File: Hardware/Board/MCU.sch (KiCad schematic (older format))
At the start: 27 parts

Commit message: Wago und FPC Libs zugefügt
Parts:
- added J?: 1-1734592-2, SamacSys_Parts:1-1734592-2, symbol SamacSys_Parts:1-1734592-2
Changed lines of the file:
@@
 Wire Wire Line
 	9300 4850 9300 4800
+$Comp
+L SamacSys_Parts:1-1734592-2 J?
+U 1 1 5CB67827
+P 7500 3050
+F 0 "J?" H 8000 3315 50  0000 C CNN
+F 1 "1-1734592-2" H 8000 3224 50  0000 C CNN
+F 2 "SamacSys_Parts:1-1734592-2" H 8350 3150 50  0001 L CNN
+F 3 "https://www.te.com/commerce/DocumentDelivery/DDEController?Action=showdoc&DocId=Customer+Drawing%7F1734592%7FC%7Fpdf%7FEnglish%7FENG_CD_1734592_C_C_1734592.pdf%7F1-1734592-2" H 8350 3050 50  0001 L CNN
+F 4 "TE Connectivity 0.5mm Pitch 12 Way Right Angle Female FPC Connector Locking Mechanism" H 8350 2950 50  0001 L CNN "Description"
+F 5 "2.3" H 8350 2850 50  0001 L CNN "Height"
+F 6 "TE Connectivity" H 8350 2750 50  0001 L CNN "Manufacturer_Name"
+F 7 "1-1734592-2" H 8350 2650 50  0001 L CNN "Manufacturer_Part_Number"
+F 8 "571-1-1734592-2" H 8350 2550 50  0001 L CNN "Mouser Part Number"
+F 9 "https://www.mouser.com/Search/Refine.aspx?Keyword=571-1-1734592-2" H 8350 2450 50  0001 L CNN "Mouser Price/Stock"
+F 10 "7188602" H 8350 2350 50  0001 L CNN "RS Part Number"
+F 11 "http://uk.rs-online.com/web/p/products/7188602" H 8350 2250 50  0001 L CNN "RS Price/Stock"
+	1    7500 3050
+	1    0    0    -1
+$EndComp
 $EndSCHEMATC

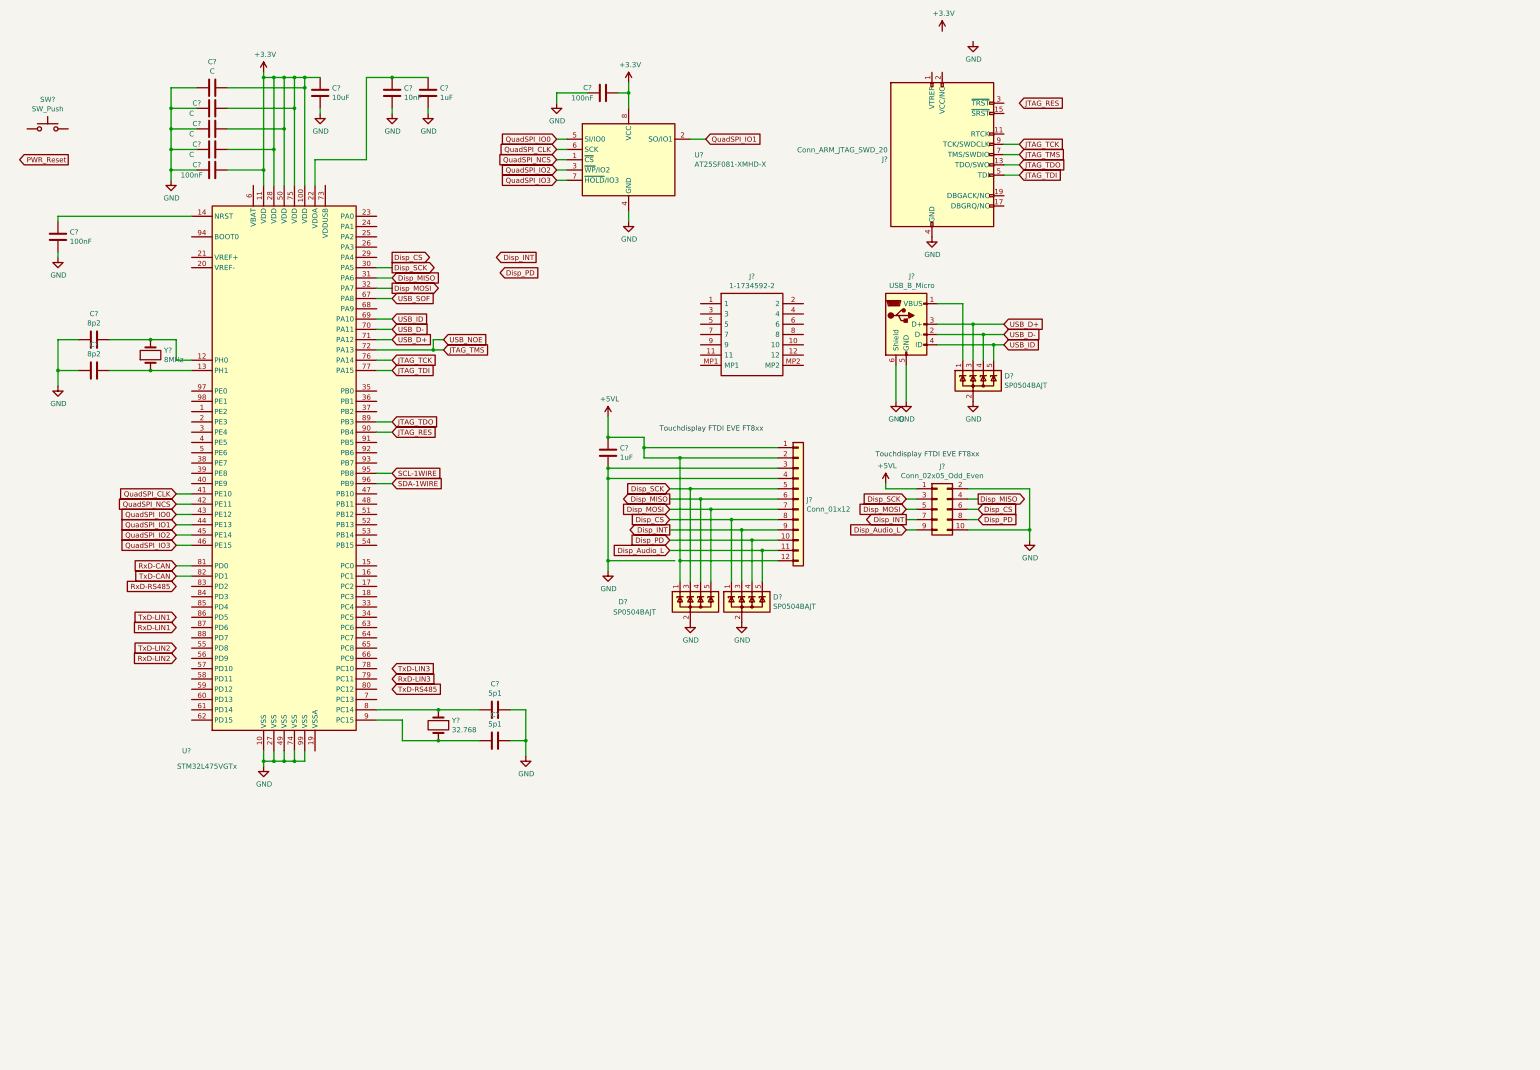
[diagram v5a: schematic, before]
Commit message: Netzliste und Board erstellt, hier sind noch Fehler im Bereich Footprints, BLE Modul nRF8001 hinzugefügt, erste Anschlussklemmen zugefügt
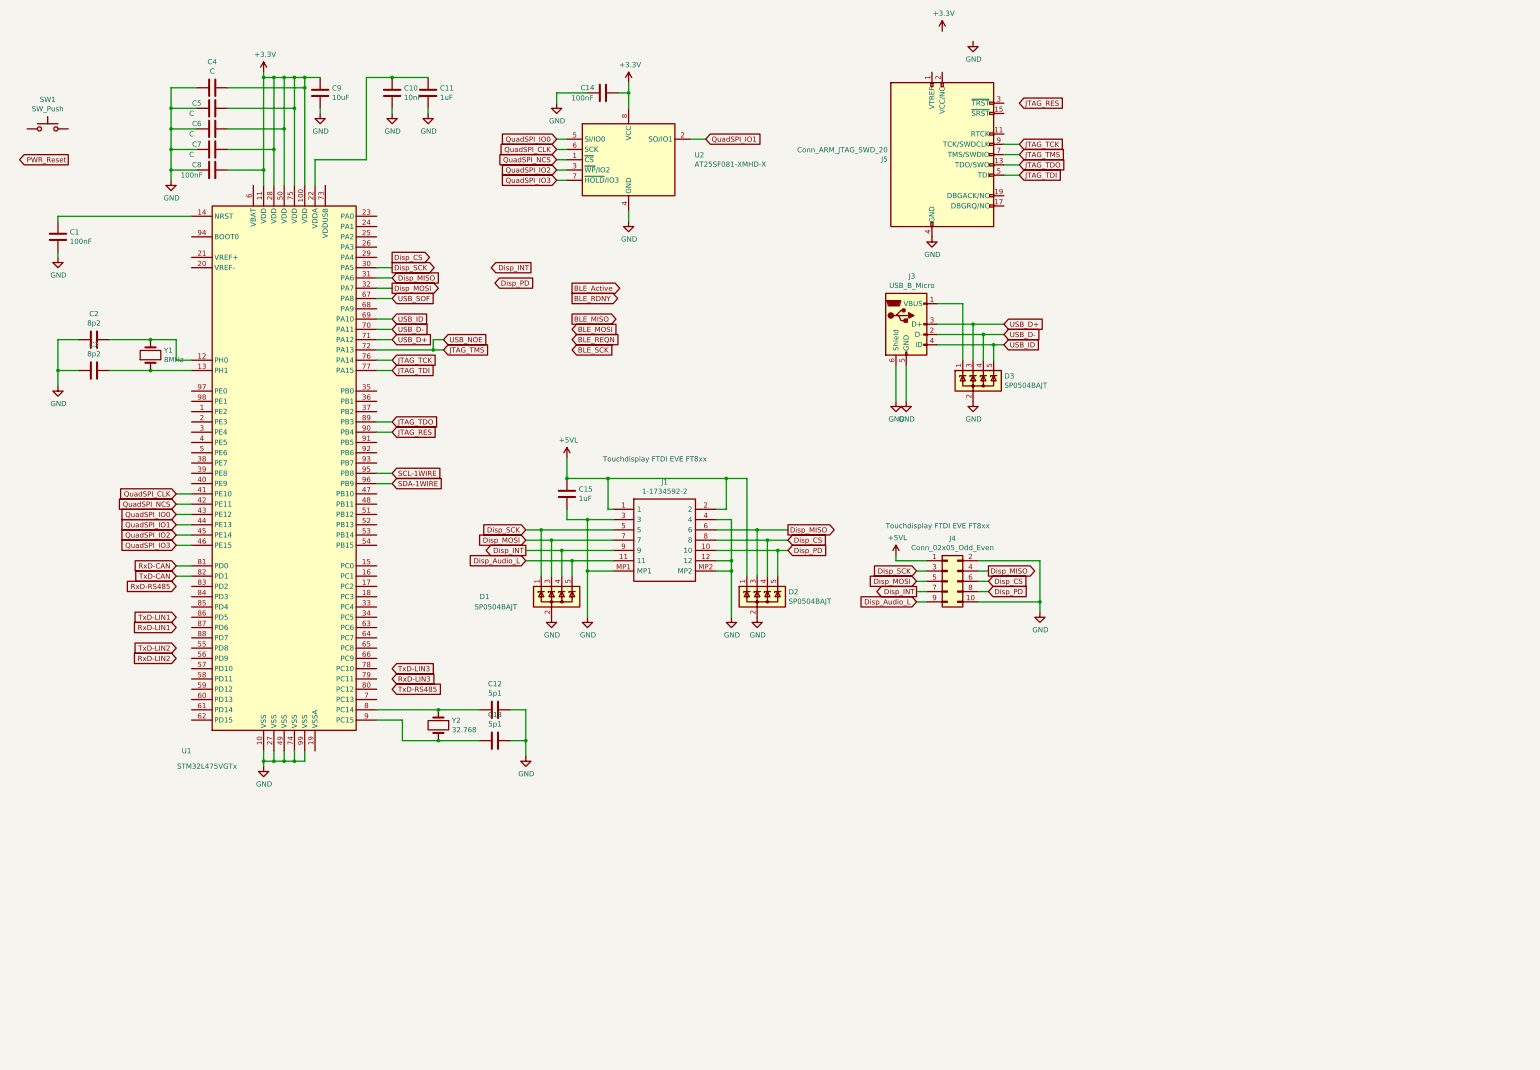
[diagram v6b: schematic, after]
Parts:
- removed J?: Conn_01x12, symbol Connector_Generic:Conn_01x12
- C1, C10, C11, C12, C13, C14, C15, C2, C3, C4, C5, C6, C7, C8: renamed from C?; footprint (none) -> Capacitor_SMD:C_0603_1608Metric
- C9: renamed from C?; footprint (none) -> Capacitor_SMD:C_1210_3225Metric
- J3: renamed from J?; footprint (none) -> Connector_USB:USB_Micro-B_Molex-105017-0001
- J4: renamed from J?; footprint (none) -> Connector_IDC:IDC-Header_2x05_P2.54mm_Vertical
- J5: renamed from J?; footprint (none) -> Connector_IDC:IDC-Header_2x10_P2.54mm_Vertical
- gave numbers to parts that had none: 9
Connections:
- net +5VL: now also D2.1 (K), J1.1, J1.2; no longer D1.1 (K)
- net Disp_Audio_L: now also D1.5 (K), J1.11; no longer D2.5 (K)
- net Disp_CS: now also D2.4 (K), J1.8; no longer D2.1 (K)
- net Disp_INT: now also D1.4 (K), J1.9; no longer D2.3 (K)
- net Disp_MISO: now also D2.3 (K), J1.6; no longer D1.4 (K)
- net Disp_MOSI: now also D1.3 (K), J1.7; no longer D1.5 (K)
- net Disp_PD: now also D2.5 (K), J1.10; no longer D2.4 (K)
- net Disp_SCK: now also D1.1 (K), J1.5; no longer D1.3 (K)
- net GND: now also J1.12, J1.3, J1.4, J1.MP1, J1.MP2
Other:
- moved on the sheet: C15, D1, D2, J1, J4

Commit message: Änderung CPU auf einen mit Display Controller, vorbereitung zum Anschluss SSD1963 und Digital RGB Displays
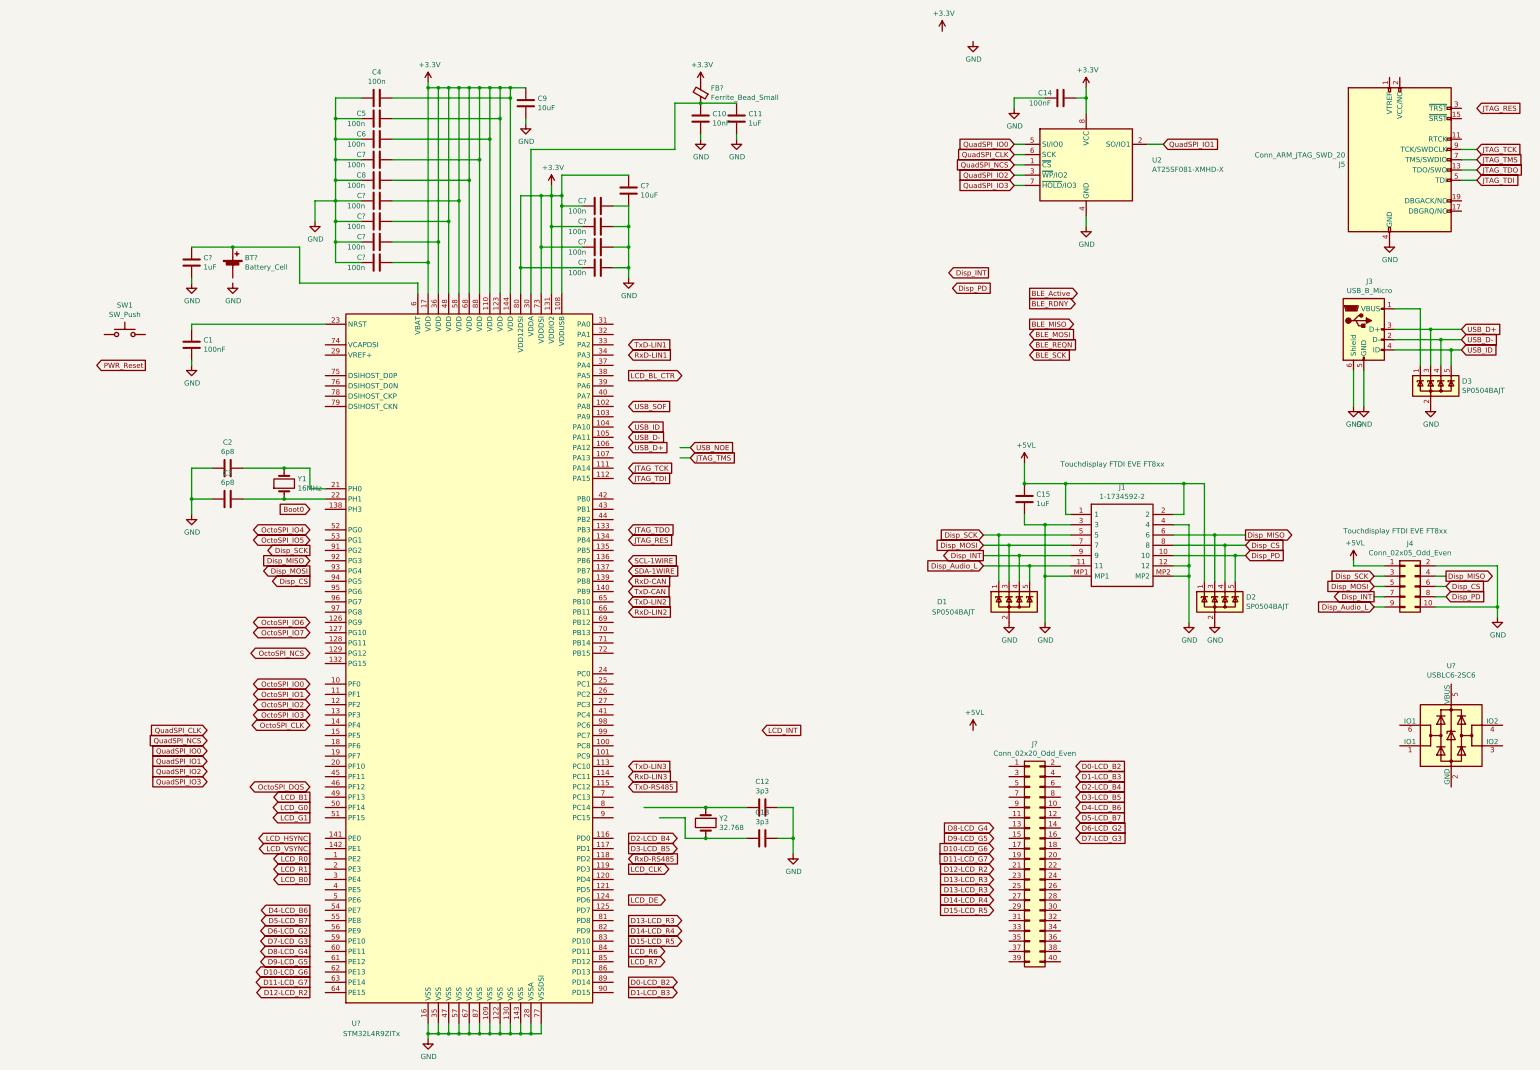
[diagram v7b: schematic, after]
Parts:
- removed U1: STM32L475VGTx, Package_QFP:LQFP-100_14x14mm_P0.5mm, symbol MCU_ST_STM32L4:STM32L475VGTx
- added BT?: Battery_Cell, symbol Device:Battery_Cell
- added C? (x8): 100n, Capacitor_SMD:C_0603_1608Metric, symbol Device:C
- added C?: 1uF, Capacitor_SMD:C_0603_1608Metric, symbol Device:C
- added C?: 10uF, Capacitor_SMD:C_1210_3225Metric, symbol Device:C
- added FB?: Ferrite_Bead_Small, symbol Device:Ferrite_Bead_Small
- added J?: Conn_02x20_Odd_Even, symbol Connector_Generic:Conn_02x20_Odd_Even
- added U?: STM32L4R9ZITx, Package_QFP:LQFP-144_20x20mm_P0.5mm, symbol MCU_ST_STM32L4+:STM32L4R9ZITx
- added U?: USBLC6-2SC6, Package_TO_SOT_SMD:SOT-23-6, symbol Power_Protection:USBLC6-2SC6
- C12, C13: value 5p1 -> 3p3
- C2, C3: value 8p2 -> 6p8
- C4, C5, C6, C7: value C -> 100n
- C8: value 100nF -> 100n
- Y1: value 8MHz -> 16MHz
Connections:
- net +3V3: now also C?.1, C?.1, C?.1, C?.1, C?.1, C?.2, C?.2, C?.2, C?.2, FB?.2, U?.108 (VDDUSB), U?.110 (VDD), U?.123 (VDD), U?.131 (VDDIO2), U?.144 (VDD), U?.17 (VDD), U?.36 (VDD), U?.48 (VDD), U?.58 (VDD), U?.68 (VDD), U?.73 (VDDDSI), U?.80 (VDD12DSI), U?.88 (VDD)
- net GND: now also C?.1, C?.1, C?.1, C?.1, C?.2, C?.2, C?.2, C?.2, C?.2, C?.2, U?.109 (VSS), U?.122 (VSS), U?.130 (VSS), U?.143 (VSS), U?.16 (VSS), U?.28 (VSSA), U?.35 (VSS), U?.47 (VSS), U?.57 (VSS), U?.67 (VSS), U?.77 (VSSDSI), U?.87 (VSS)
- net at C2.1, Y1.2: now also U?.21 (PH0)
- net at C3.1, Y1.1: now also U?.22 (PH1)
- net at C1.1: now also U?.23 (NRST)
- net at C10.1, C11.1: now also FB?.1, U?.30 (VDDA)
- new net: BT?.1 (+), C?.1, U?.6 (VBAT)
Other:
- moved on the sheet: C1, C10, C11, C12, C13, C14, C15, C2, C3, C4, C5, C6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

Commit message: Display auf 40 Pin FPC reduziert, nur Verwendung des internen Display Controllers, Library Updates
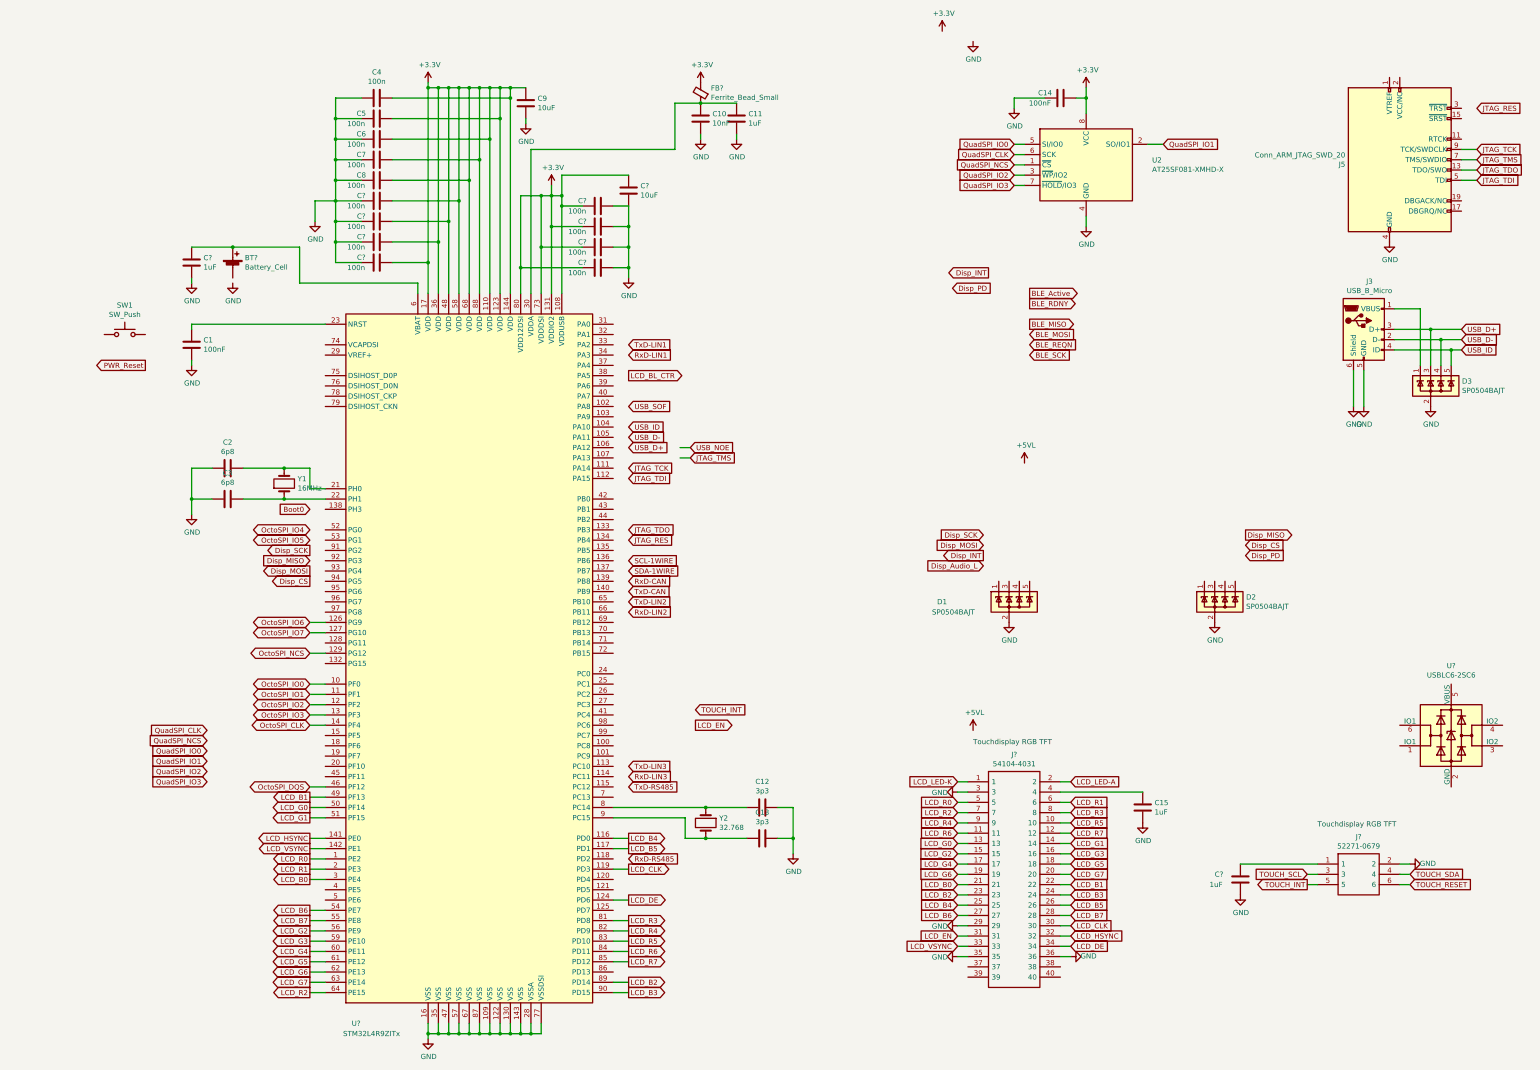
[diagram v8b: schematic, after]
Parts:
- removed J1: 1-1734592-2, SamacSys_Parts:1-1734592-2, symbol SamacSys_Parts:1-1734592-2
- removed J4: Conn_02x05_Odd_Even, Connector_IDC:IDC-Header_2x05_P2.54mm_Vertical, symbol Connector_Generic:Conn_02x05_Odd_Even
- removed J?: Conn_02x20_Odd_Even, symbol Connector_Generic:Conn_02x20_Odd_Even
- added C?: 1uF, Capacitor_SMD:C_0603_1608Metric, symbol Device:C
- added J?: 54104-4031, 54104-4031, symbol SamacSys_Parts:54104-4031
- added J?: 52271-0679, 52271-0679, symbol SamacSys_Parts:52271-0679
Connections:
- net +5VL: no longer C15.1, D2.1 (K)
- net Disp_Audio_L: no longer D1.5 (K)
- net Disp_CS: no longer D2.4 (K)
- net Disp_INT: no longer D1.4 (K)
- net Disp_MISO: no longer D2.3 (K)
- net Disp_MOSI: no longer D1.3 (K)
- net Disp_PD: no longer D2.5 (K)
- net Disp_SCK: no longer D1.1 (K)
- net GND: now also C?.2, J?.2, J?.29, J?.3, J?.35, J?.36
- net LCD_B0: now also U?.3 (PE4), J?.21
- net LCD_B1: now also U?.49 (PF13), J?.22
- net LCD_CLK: now also U?.119 (PD3), J?.30
- net LCD_DE: now also U?.124 (PD6), J?.34
- net LCD_G0: now also U?.50 (PF14), J?.13
- net LCD_G1: now also U?.51 (PF15), J?.14
- net LCD_HSYNC: now also U?.141 (PE0), J?.32
- net LCD_R0: now also U?.1 (PE2), J?.5
- net LCD_R1: now also U?.2 (PE3), J?.6
- net LCD_R6: now also U?.84 (PD11), J?.11
- net LCD_R7: now also U?.85 (PD12), J?.12
- net LCD_VSYNC: now also U?.142 (PE1), J?.33
- net OctoSPI_CLK: now also U?.14 (PF4)
- net OctoSPI_DQS: now also U?.46 (PF12)
- net OctoSPI_IO0: now also U?.10 (PF0)
- net OctoSPI_IO1: now also U?.11 (PF1)
- net OctoSPI_IO2: now also U?.12 (PF2)
- net OctoSPI_IO3: now also U?.13 (PF3)
- net OctoSPI_IO6: now also U?.126 (PG9)
- net OctoSPI_IO7: now also U?.127 (PG10)
- net OctoSPI_NCS: now also U?.129 (PG12)
- net at C12.2, Y2.1: now also U?.8 (PC14)
- net at C13.2, Y2.2: now also U?.9 (PC15)
- net LCD_B4: now reaches U?.116 (PD0)
- net LCD_B4: now also J?.25
- net LCD_B5: now reaches U?.117 (PD1)
- net LCD_B5: now also J?.26
- net LCD_B6: now reaches U?.54 (PE7)
- net LCD_B6: now also J?.27
- net LCD_B7: now reaches U?.55 (PE8)
- net LCD_B7: now also J?.28
- net LCD_G2: now reaches U?.56 (PE9)
- net LCD_G2: now also J?.15
- net LCD_G3: now reaches U?.59 (PE10)
- net LCD_G3: now also J?.16
- net LCD_G4: now reaches U?.60 (PE11)
- net LCD_G4: now also J?.17
- net LCD_G5: now reaches U?.61 (PE12)
- net LCD_G5: now also J?.18
- net LCD_G6: now reaches U?.62 (PE13)
- net LCD_G6: now also J?.19
- net LCD_G7: now reaches U?.63 (PE14)
- net LCD_G7: now also J?.20
- net LCD_R2: now reaches U?.64 (PE15)
- net LCD_R2: now also J?.7
- net LCD_R3: now reaches U?.81 (PD8)
- net LCD_R3: now also J?.8
- net LCD_R4: now reaches U?.82 (PD9)
- net LCD_R4: now also J?.9
- net LCD_R5: now reaches U?.83 (PD10)
- net LCD_R5: now also J?.10
- net LCD_B2: now reaches U?.89 (PD14)
- net LCD_B2: now also J?.23
- net LCD_B3: now reaches U?.90 (PD15)
- net LCD_B3: now also J?.24
- new net: C15.1, J?.4
- new net: C?.1, J?.1
- new net LCD_EN: J?.31
- new net LCD_LED-A: J?.2
- new net LCD_LED-K: J?.1
- new net TOUCH_INT: J?.5
- new net TOUCH_RESET: J?.6
- new net TOUCH_SCL: J?.3
- new net TOUCH_SDA: J?.4
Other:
- note added: "Touchdisplay RGB TFT"
- note removed: "Touchdisplay FTDI EVE FT8xx"
- moved on the sheet: C15
